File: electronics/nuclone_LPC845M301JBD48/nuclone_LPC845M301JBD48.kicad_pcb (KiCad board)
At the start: 2 copper layers, 48.3 x 76.2 mm, 53 parts, among them J1 JTAG_2X05, J2 USB-ID, J3 nuclone_small_left, J4 nuclone_small_right, SW1 RESET, U1 MCP1702-MB, U2 LPC845M301JBD48, Y1 12MHz

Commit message: routed more power busses and gpios
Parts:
- moved JP5 4.04 mm to (93.2, 90.7)
- moved JP4 3.91 mm to (93.2, 89.4)
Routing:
- net /VDD: track 84.2 -> 107.8 mm, vias 3 -> 4
- net /VREFP: track 0.00 -> 6.78 mm, vias 0 -> 1
- net /VREFN: track 0.00 -> 6.66 mm, vias 0 -> 1
- net /PIO0_7: track 0.00 -> 5.48 mm
- net /PIO1_7: track 0.00 -> 5.48 mm
- net /PIO0_6: track 0.00 -> 5.48 mm
- net /PIO0_0: track 0.00 -> 5.45 mm
- net /VSS: track 20.7 -> 25.9 mm, vias 8 -> 9
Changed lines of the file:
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@@
     (thickness 1.6)
     (drawings 8)
-    (tracks 357)
+    (tracks 403)
     (zones 0)
     (modules 53)
@@
   )
   (setup
-    (last_trace_width 0.3)
+    (last_trace_width 0.4)
     (user_trace_width 0.15)
     (user_trace_width 0.2)
@@
   )
   (module SquantorSpecial:solder_jumper_2way_conn (layer B.Cu)
-    (at 89.45 89.2)
+    (at 93.2 90.7)
     (descr "Resistor SMD 0402, reflow soldering, Vishay (see dcrcw.pdf)")
     (tags "resistor 0402")
@@
   )
   (module SquantorSpecial:solder_jumper_2way_conn (layer B.Cu)
-    (at 89.45 90.5)
+    (at 93.2 89.4)
     (descr "Resistor SMD 0402, reflow soldering, Vishay (see dcrcw.pdf)")
     (tags "resistor 0402")
@@
   (segment (start 106.68 74.93) (end 104.14 74.93) (width 0.6) (layer F.Cu) (net 4))
   (segment (start 104.14 74.93) (end 104.07 75) (width 0.6) (layer F.Cu) (net 4))
-  (segment (start 104.07 75) (end 92 75) (width 0.6) (layer F.Cu) (net 4))
   (via (at 92 75) (size 0.95) (drill 0.8) (layers F.Cu B.Cu) (net 4))
   (segment (start 88.8 73) (end 89.8 72) (width 0.6) (layer F.Cu) (net 4))
@@
   (segment (start 88.4 72.6) (end 88.8 73) (width 0.4) (layer F.Cu) (net 4))
   (segment (start 86.45 72.6) (end 88.4 72.6) (width 0.4) (layer F.Cu) (net 4))
-  (via (at 84.3 74) (size 0.65) (drill 0.4) (layers F.Cu B.Cu) (net 4))
   (segment (start 84.3 74) (end 83.1 74) (width 0.6) (layer F.Cu) (net 4))
   (segment (start 87.8 74) (end 84.3 74) (width 0.6) (layer F.Cu) (net 4))
+  (segment (start 89.525 92.15) (end 91.75 92.15) (width 0.3) (layer F.Cu) (net 4))
+  (segment (start 92.35 92.75) (end 92.8 92.75) (width 0.3) (layer F.Cu) (net 4))
+  (segment (start 91.75 92.15) (end 92.35 92.75) (width 0.3) (layer F.Cu) (net 4))
+  (segment (start 93.9 92.75) (end 92.8 92.75) (width 0.4) (layer F.Cu) (net 4))
+  (segment (start 93.9 92.75) (end 94.95 92.75) (width 0.4) (layer F.Cu) (net 4))
+  (segment (start 94.95 92.75) (end 95.5 92.2) (width 0.4) (layer F.Cu) (net 4))
+  (via (at 95.5 89.5) (size 0.6) (drill 0.3) (layers F.Cu B.Cu) (net 4))
+  (segment (start 95.5 92.2) (end 95.5 89.5) (width 0.4) (layer F.Cu) (net 4))
+  (via (at 95.5 75) (size 0.6) (drill 0.3) (layers F.Cu B.Cu) (net 4))
+  (segment (start 95.5 89.5) (end 95.5 75) (width 0.4) (layer B.Cu) (net 4))
+  (segment (start 95.5 75) (end 92 75) (width 0.6) (layer F.Cu) (net 4))
+  (segment (start 104.07 75) (end 95.5 75) (width 0.6) (layer F.Cu) (net 4))
   (segment (start 71.1 66.1) (end 71.1 67.65) (width 0.4) (layer F.Cu) (net 5))
   (segment (start 71.16 66.04) (end 71.1 66.1) (width 0.4) (layer F.Cu) (net 5))
@@
   (via (at 78.9 72.6) (size 0.6) (drill 0.3) (layers F.Cu B.Cu) (net 11))
   (segment (start 79.75 72.6) (end 78.9 72.6) (width 0.4) (layer F.Cu) (net 11))
+  (segment (start 89.525 91.65) (end 92.8 91.65) (width 0.3) (layer F.Cu) (net 11))
+  (segment (start 93.9 91.65) (end 92.8 91.65) (width 0.4) (layer F.Cu) (net 11))
+  (via (at 94.7 91.7) (size 0.6) (drill 0.3) (layers F.Cu B.Cu) (net 11))
+  (segment (start 94.65 91.65) (end 94.7 91.7) (width 0.4) (layer F.Cu) (net 11))
+  (segment (start 93.9 91.65) (end 94.65 91.65) (width 0.4) (layer F.Cu) (net 11))
   (segment (start 72.4 66.06) (end 72.4 67.65) (width 0.4) (layer F.Cu) (net 12))
   (segment (start 72.43 66.03) (end 72.4 66.06) (width 0.4) (layer F.Cu) (net 12))
@@
   (segment (start 71.1 77.5) (end 71.1 75.9) (width 0.2) (layer F.Cu) (net 36))
   (via (at 79.8 87.4) (size 0.6) (drill 0.3) (layers F.Cu B.Cu) (net 36))
+  (segment (start 92 88.2) (end 94.4 88.2) (width 0.2) (layer F.Cu) (net 37))
+  (segment (start 90.55 89.65) (end 92 88.2) (width 0.2) (layer F.Cu) (net 37))
+  (segment (start 89.525 89.65) (end 90.55 89.65) (width 0.2) (layer F.Cu) (net 37))
+  (segment (start 94.3 88.7) (end 94.4 88.7) (width 0.2) (layer F.Cu) (net 38))
+  (segment (start 92.1 88.7) (end 94.3 88.7) (width 0.2) (layer F.Cu) (net 38))
+  (segment (start 90.65 90.15) (end 92.1 88.7) (width 0.2) (layer F.Cu) (net 38))
+  (segment (start 89.525 90.15) (end 90.65 90.15) (width 0.2) (layer F.Cu) (net 38))
   (segment (start 64.79 83.8) (end 63.5 85.09) (width 0.2) (layer F.Cu) (net 39))
   (segment (start 67.9 83.8) (end 64.79 83.8) (width 0.2) (layer F.Cu) (net 39))
@@
   (segment (start 67.07 113.03) (end 66.04 113.03) (width 0.2) (layer F.Cu) (net 45))
   (segment (start 77.4 102.7) (end 67.07 113.03) (width 0.2) (layer F.Cu) (net 45))
+  (segment (start 89.525 88.59) (end 90.41 88.59) (width 0.2) (layer F.Cu) (net 46))
+  (segment (start 90.41 88.59) (end 91.8 87.2) (width 0.2) (layer F.Cu) (net 46))
+  (segment (start 91.8 87.2) (end 94.4 87.2) (width 0.2) (layer F.Cu) (net 46))
   (segment (start 82.29 95.825) (end 82.29 96.81) (width 0.2) (layer F.Cu) (net 47))
   (segment (start 82.29 96.81) (end 82 97.1) (width 0.2) (layer F.Cu) (net 47))
@@
   (segment (start 93.1 100.7) (end 95.3 102.9) (width 0.2) (layer F.Cu) (net 49))
   (segment (start 93.1 98.7) (end 93.1 100.7) (width 0.2) (layer F.Cu) (net 49))
+  (segment (start 91.9 87.7) (end 94.4 87.7) (width 0.2) (layer F.Cu) (net 50))
+  (segment (start 90.45 89.15) (end 91.9 87.7) (width 0.2) (layer F.Cu) (net 50))
+  (segment (start 89.525 89.15) (end 90.45 89.15) (width 0.2) (layer F.Cu) (net 50))
   (segment (start 89.525 92.65) (end 91.45 92.65) (width 0.2) (layer F.Cu) (net 51))
   (segment (start 91.45 92.65) (end 92.8 94) (width 0.2) (layer F.Cu) (net 51))
@@
   (segment (start 68.19 94.21) (end 67.15 95.25) (width 0.2) (layer F.Cu) (net 58))
   (segment (start 80.675 94.21) (end 68.19 94.21) (width 0.2) (layer F.Cu) (net 58))
+  (segment (start 89.525 91.15) (end 91.65 91.15) (width 0.3) (layer F.Cu) (net 59))
+  (segment (start 92.25 90.55) (end 92.8 90.55) (width 0.3) (layer F.Cu) (net 59))
+  (segment (start 91.65 91.15) (end 92.25 90.55) (width 0.3) (layer F.Cu) (net 59))
+  (segment (start 92.8 90.55) (end 93.9 90.55) (width 0.4) (layer F.Cu) (net 59))
+  (via (at 94.7 90.4) (size 0.6) (drill 0.3) (layers F.Cu B.Cu) (net 59))
+  (segment (start 94.55 90.55) (end 94.7 90.4) (width 0.4) (layer F.Cu) (net 59))
+  (segment (start 93.9 90.55) (end 94.55 90.55) (width 0.4) (layer F.Cu) (net 59))
+  (segment (start 94.4 90.7) (end 93.65 90.7) (width 0.4) (layer B.Cu) (net 59))
+  (segment (start 94.7 90.4) (end 94.4 90.7) (width 0.4) (layer B.Cu) (net 59))
+  (segment (start 89.525 90.65) (end 91.05 90.65) (width 0.3) (layer F.Cu) (net 60))
+  (segment (start 92.25 89.45) (end 92.8 89.45) (width 0.3) (layer F.Cu) (net 60))
+  (segment (start 91.05 90.65) (end 92.25 89.45) (width 0.3) (layer F.Cu) (net 60))
+  (segment (start 92.8 89.45) (end 93.9 89.45) (width 0.4) (layer F.Cu) (net 60))
+  (via (at 94.7 89.5) (size 0.6) (drill 0.3) (layers F.Cu B.Cu) (net 60))
+  (segment (start 94.65 89.45) (end 94.7 89.5) (width 0.4) (layer F.Cu) (net 60))
+  (segment (start 93.9 89.45) (end 94.65 89.45) (width 0.4) (layer F.Cu) (net 60))
+  (segment (start 94.6 89.4) (end 93.65 89.4) (width 0.4) (layer B.Cu) (net 60))
+  (segment (start 94.7 89.5) (end 94.6 89.4) (width 0.4) (layer B.Cu) (net 60))
   (segment (start 83.95 72.6) (end 85.35 72.6) (width 0.4) (layer F.Cu) (net 63))
   (segment (start 83 70) (end 83 68.79748) (width 0.4) (layer F.Cu) (net 68))

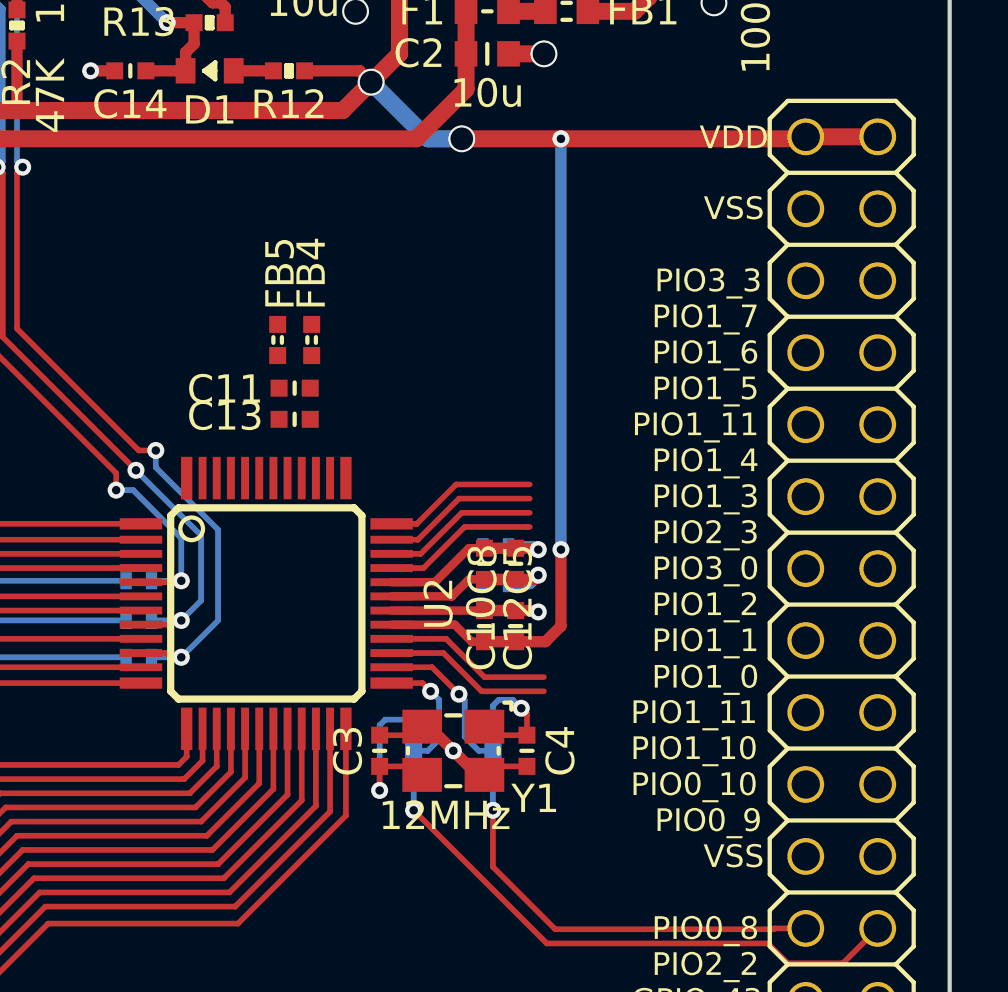
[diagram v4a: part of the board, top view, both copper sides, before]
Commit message: WIP routing pins and some power networks
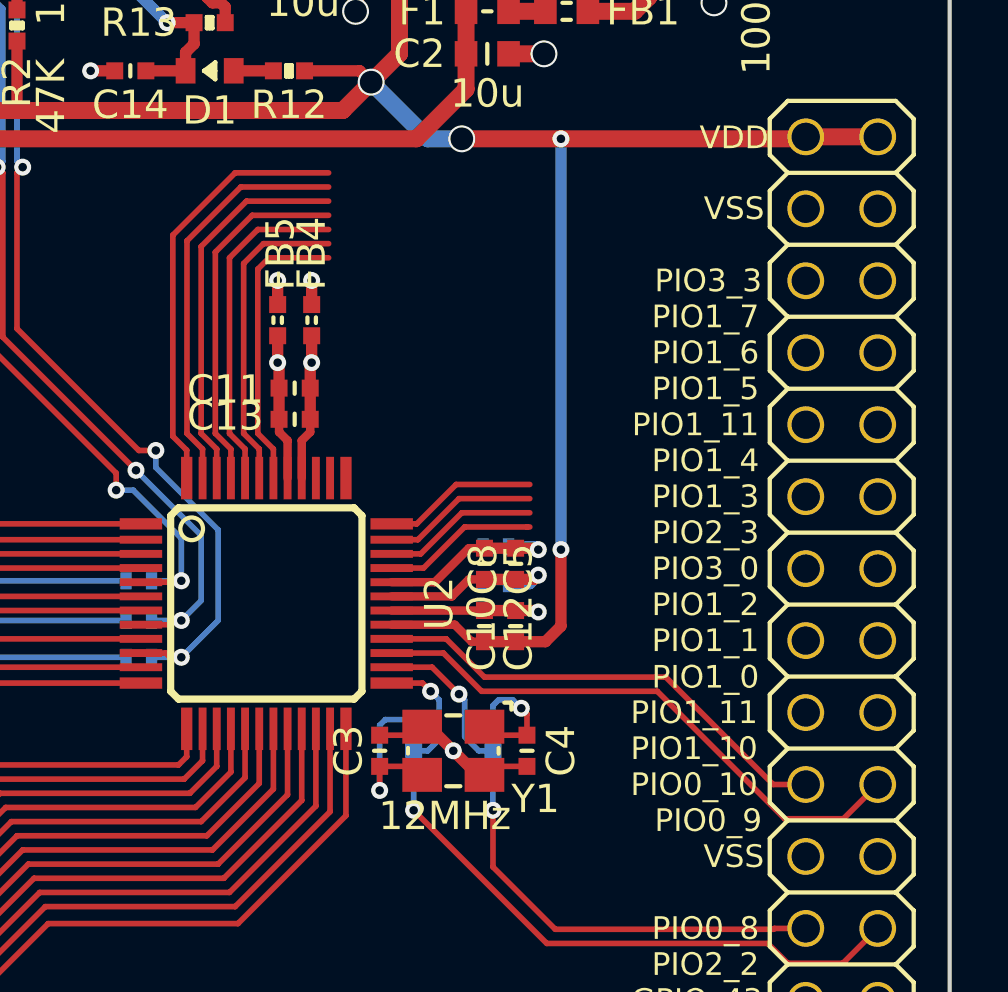
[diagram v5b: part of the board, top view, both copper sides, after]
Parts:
- moved FB4 0.70 mm to (86.7, 81.4)
- moved FB5 0.70 mm to (85.5, 81.4)
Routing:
- net /PIO0_17: track 0.00 -> 15.2 mm
- net /PIO0_18: track 0.00 -> 14.4 mm
- net /PIO1_5: track 5.93 -> 20.1 mm
- net /PIO0_19: track 0.00 -> 13.6 mm
- net /PIO0_20: track 0.00 -> 12.7 mm
- net /PIO0_21: track 0.00 -> 11.9 mm
- net /PIO0_22: track 0.00 -> 11.1 mm
- net /PIO1_6: track 5.93 -> 16.7 mm
- net /PIO0_30: track 0.00 -> 10.3 mm
- net /VDDA: track 0.00 -> 5.17 mm, vias 0 -> 1
- net /VSSA: track 0.00 -> 5.17 mm, vias 0 -> 1
- net /VSS: track 25.9 -> 26.8 mm, vias 9 -> 10
- net /VDD: track 107.8 -> 108.7 mm, vias 4 -> 5

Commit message: all airwires routed
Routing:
- net /PIO0_23: track 0.00 -> 24.0 mm
- net /PIO0_14: track 0.00 -> 23.1 mm
- net /PIO0_22: track 11.1 -> 34.2 mm
- net /PIO0_20: track 12.7 -> 35.2 mm
- net /PIO0_18: track 14.4 -> 36.2 mm
- net /PIO0_29: track 0.00 -> 20.5 mm
- net /PIO0_30: track 10.3 -> 30.6 mm
- net /PIO0_21: track 11.9 -> 31.6 mm
- net /PIO0_19: track 13.6 -> 32.6 mm
- net /PIO0_17: track 15.2 -> 33.6 mm
- net /PIO0_7: track 5.48 -> 21.5 mm
- net /PIO1_7: track 5.48 -> 20.8 mm
- net /VSSA: track 5.17 -> 19.4 mm
- net /PIO0_6: track 5.48 -> 18.1 mm
- net /PIO0_0: track 5.45 -> 17.5 mm
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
